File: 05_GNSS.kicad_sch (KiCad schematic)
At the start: 0 parts

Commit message: updated schematics
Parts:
- added U8: MAX-F10S-00B, MAX-F10S_UBL, symbol 2026-09-16_06-45-24:MAX-F10S-00B
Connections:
- new net GND: U8.1 (GND), U8.10 (GND), U8.12 (GND), U8.15 (VIO_SEL)
- new net GNSS_EXTINT: U8.5 (EXTINT)
- new net GNSS_RF: U8.11 (RF_IN)
- new net GNSS_TIMEPULSE: U8.4 (TIMEPULSE)
- new net GNSS_UART_RX: U8.3 (RXD)
- new net GNSS_UART_TX: U8.2 (TXD)
- new net VOUT1_1V8: U8.7 (V_IO)
- new net VOUT2_3V0_PROVISIONAL: U8.8 (VCC)
- no-connect marks 0 -> 7
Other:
- note added: "05_GNSS — u-blox MAX-F10S-00B DUAL-BAND GNSS — REV A"
- note added: "EXTINT is routed as an optional host signal for wake/time assistance. Final Apollo pin allocation may omit it if UART-RX wake is sufficient."
- note added: "Footprint field MAX-F10S_UBL is retained from the imported symbol; verify module pad geometry, pin-1 orientation and courtyard during the footprint audit."
- note added: "If VCC/V_IO are ever hard-switched off, Apollo pins connected to MAX-F10S must be Hi-Z first; do not drive GNSS I/O while its supplies are absent."
- note added: "MAX-F10S integrates L1/L5 SAW filtering + LNA + diplexer SAW, so do not duplicate an external SAW/LNA stage without a measured RF reason."
- note added: "POWER MANAGEMENT: prefer MAX-F10S software-standby when GNSS is idle. VCC and V_IO remain supplied, so host PIO isolation buffers are not required."
- note added: "POWER: VCC = VOUT2_3V0_PROVISIONAL (~3.0 V); V_IO = VOUT1_1V8; VIO_SEL = GND selects the 1.8 V I/O range."
- note added: "Primary host link = UART at 1.8 V logic. Passive L1/L5 antenna is the Rev-A baseline; RF network is finished on 14_RF."
- note added: "RESET_N is intentionally NC. u-blox recommends leaving it open for normal operation; do not add a capacitor to RESET_N. Reset also clears BBR/RTC/orbit data."
- note added: "RF_IN -> GNSS_RF. Route as controlled 50 ohm; RF_IN already contains a DC block. Keep this trace extremely short and away from display/Wi-Fi/high-speed clocks."
- note added: "SDA/SCL and SAFEBOOT_N are NC because UART is the primary host interface. LNA_EN and VCC_RF are NC for the passive-antenna baseline."
- note added: "TIMEPULSE is routed to GNSS_TIMEPULSE. Never load/pull it low during receiver startup because it is internally linked to SAFEBOOT_N."
- note added: "The 1.8 V V_IO rail must meet u-blox ±2% accuracy. VCC supply path must support up to 100 mA startup inrush and must not add >0.2 ohm series resistance."
- note added: "VOUT1_1V8 / VOUT2_3V0_PROVISIONAL and host/RF labels are local to this child sheet until the final hierarchy integration pass."
- note added: "V_BCKP is intentionally NC in Rev A. Host time/orbit assistance can be used instead; add a backup rail later only if TTFF measurements justify it."
- title: (none) -> Rev-A — GNSS

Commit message: refactor(kicad): integrate Rev-A hierarchy and libraries
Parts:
- U8: footprint MAX-F10S_UBL -> sportwatch_custom:MAX-F10S_UBL
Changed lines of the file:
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@@
 		)
 	)
-	(label "GNSS_TIMEPULSE"
+	(hierarchical_label "GNSS_TIMEPULSE"
+		(shape output)
 		(at 96 99.06 180)
 		(effects
@@
 		)
 	)
-	(label "VOUT1_1V8"
+	(hierarchical_label "VOUT1_1V8"
+		(shape passive)
 		(at 96 106.68 180)
 		(effects
@@
 		)
 	)
-	(label "VOUT2_3V0_PROVISIONAL"
+	(hierarchical_label "VOUT2_3V0_PROVISIONAL"
+		(shape passive)
 		(at 96 109.22 180)
 		(effects
@@
 		)
 	)
-	(label "GNSS_UART_RX"
+	(hierarchical_label "GNSS_UART_RX"
+		(shape input)
 		(at 96 96.52 180)
 		(effects
@@
 		)
 	)
-	(label "GNSS_UART_TX"
+	(hierarchical_label "GNSS_UART_TX"
+		(shape output)
 		(at 96 93.98 180)
 		(effects
@@
 		)
 	)
-	(label "GNSS_RF"
+	(hierarchical_label "GNSS_RF"
+		(shape passive)
 		(at 194 109.22 0)
 		(effects
@@
 		)
 	)
-	(label "GNSS_EXTINT"
+	(hierarchical_label "GNSS_EXTINT"
+		(shape input)
 		(at 96 101.6 180)
 		(effects
@@
 			)
 		)
-		(property "Footprint" "MAX-F10S_UBL"
+		(property "Footprint" "sportwatch_custom:MAX-F10S_UBL"
 			(at 111.76 91.44 0)
 			(hide yes)

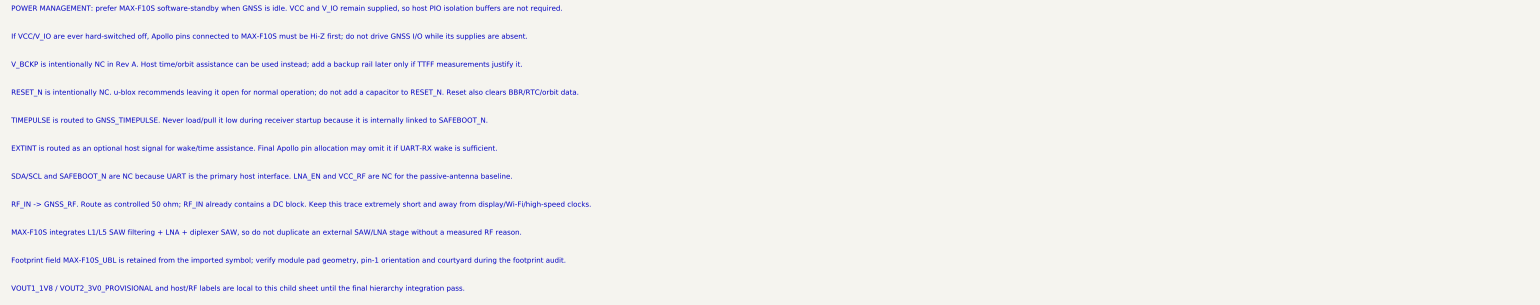
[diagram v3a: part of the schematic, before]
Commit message: fix(pcb): Round 3 foundation correction — 0 DRC errors, stacked microvias, PPG ECO & guards
- Eliminate 24 committed DRC errors by refilling all zones and committing refilled state
- Rebuild 12 L1->L3 skip microvias as 24 stackup-compliant stacked L1->L2 + L2->L3 microvias (VIPPO IPC-4761 Type VII)
- Harmonize HighSpeed_50R track width to 0.100 mm across .kicad_pro, .kicad_dru, and live copper
- Execute controlled schematic ECO swapping D413 and D424 detector channels, eliminating Jordan curve crossing
- Route all 4 PPG detector channels pad-to-pad on B.Cu with continuous dedicated PD_GND ground guards
- Close schematic residuals: Y101 MPN ABS07-32.768KHZ-6-T and 8.2pF load caps, cite primary sources for Y102 and Y1 on-chip trim, cite u-blox manual for U8 VCC_RF NC
- Formally defer staged passives (eMMC interface, PPG VLED, C206) with documented reserved placement corridors
- Document comprehensive Round 3 report and update Apollo/eMMC escape matrices and AGENT_HANDOFF.md
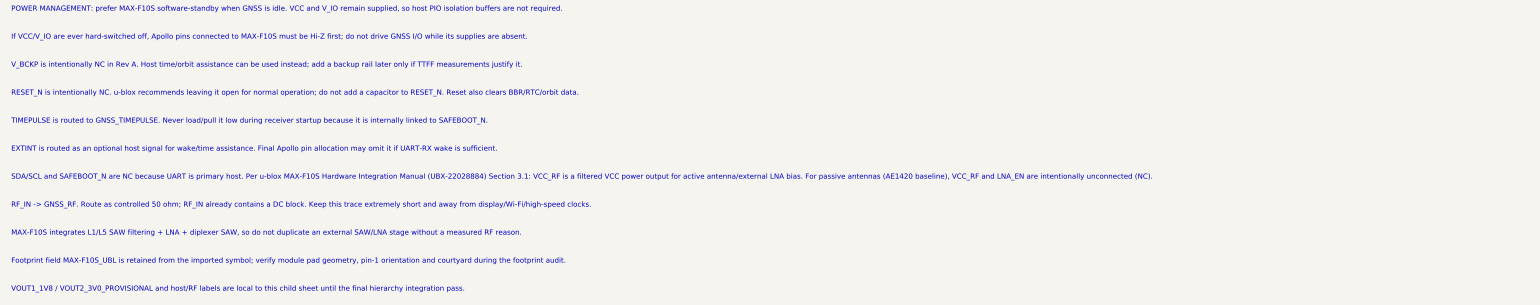
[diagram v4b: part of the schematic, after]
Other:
- note added: "SDA/SCL and SAFEBOOT_N are NC because UART is primary host. Per u-blox MAX-F10S Hardware Integration Manual (UBX-22028884) Section 3.1: VCC_RF is a filtered VCC power output for active antenna/external LNA bias. For passive antennas (AE1420 baseline), VCC_RF and LNA_EN are intentionally unconnected (NC)."
- note removed: "SDA/SCL and SAFEBOOT_N are NC because UART is the primary host interface. LNA_EN and VCC_RF are NC for the passive-antenna baseline."
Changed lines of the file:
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@@
 		)
 	)
-	(text "SDA/SCL and SAFEBOOT_N are NC because UART is the primary host interface. LNA_EN and VCC_RF are NC for the passive-antenna baseline."
+	(text "SDA/SCL and SAFEBOOT_N are NC because UART is primary host. Per u-blox MAX-F10S Hardware Integration Manual (UBX-22028884) Section 3.1: VCC_RF is a filtered VCC power output for active antenna/external LNA bias. For passive antennas (AE1420 baseline), VCC_RF and LNA_EN are intentionally unconnected (NC)."
 		(exclude_from_sim no)
 		(at 24 176 0)

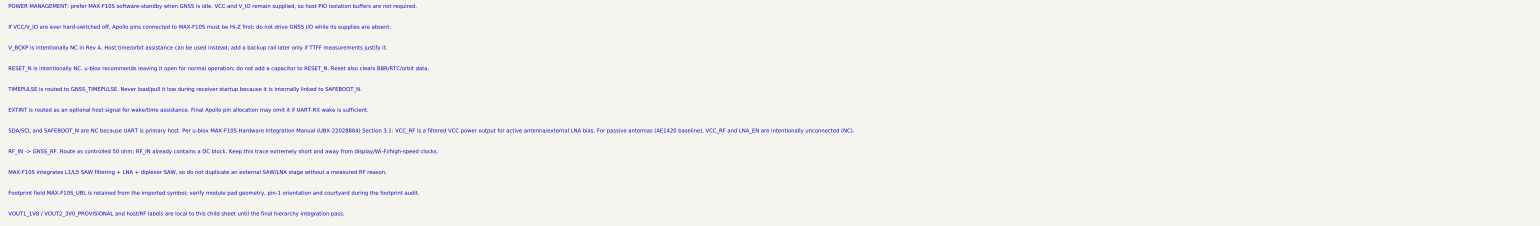
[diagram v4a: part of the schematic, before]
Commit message: fix(pcb): foundation correction round 4 closure
- Y101: select Abracon ABS06-32.768KHZ-6-1-T (2012-class SMD crystal) matching 2012 footprint
- Y101/C118/C119: rotate Y101 180 deg to align XO32 West and XI32 East; uncrossed planar routing
- Parity: synchronize C118, C119, Y101, Y102, Y1 values between schematic and PCB (0 mismatches)
- PPG guards: close NT401.2 and NT402.2 to In6.Cu GND plane via B.Cu microvias (4 channels complete)
- Rules: reconcile HighSpeed_50R track_width to 0.100 mm in .kicad_pro; refine *1V8* to *VOUT*1V8*
- GNSS: update note to cite MAX-F10S Integration Manual UBXDOC-963802114-12892 R01 and south RF_IN
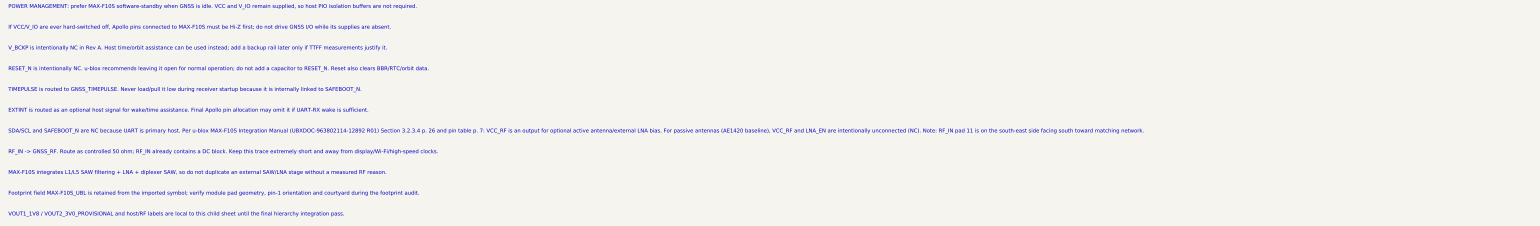
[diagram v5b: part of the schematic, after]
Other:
- note added: "SDA/SCL and SAFEBOOT_N are NC because UART is primary host. Per u-blox MAX-F10S Integration Manual (UBXDOC-963802114-12892 R01) Section 3.2.3.4 p. 26 and pin table p. 7: VCC_RF is an output for optional active antenna/external LNA bias. For passive antennas (AE1420 baseline), VCC_RF and LNA_EN are intentionally unconnected (NC). Note: RF_IN pad 11 is on the south-east side facing south toward mat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"
- note removed: "SDA/SCL and SAFEBOOT_N are NC because UART is primary host. Per u-blox MAX-F10S Hardware Integration Manual (UBX-22028884) Section 3.1: VCC_RF is a filtered VCC power output for active antenna/external LNA bias. For passive antennas (AE1420 baseline), VCC_RF and LNA_EN are intentionally unconnected (NC)."
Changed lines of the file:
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@@
 		)
 	)
-	(text "SDA/SCL and SAFEBOOT_N are NC because UART is primary host. Per u-blox MAX-F10S Hardware Integration Manual (UBX-22028884) Section 3.1: VCC_RF is a filtered VCC power output for active antenna/external LNA bias. For passive antennas (AE1420 baseline), VCC_RF and LNA_EN are intentionally unconnected (NC)."
+	(text "SDA/SCL and SAFEBOOT_N are NC because UART is primary host. Per u-blox MAX-F10S Integration Manual (UBXDOC-963802114-12892 R01) Section 3.2.3.4 p. 26 and pin table p. 7: VCC_RF is an output for optional active antenna/external LNA bias. For passive antennas (AE1420 baseline), VCC_RF and LNA_EN are intentionally unconnected (NC). Note: RF_IN pad 11 is on the south-east side facing south toward matching network."
 		(exclude_from_sim no)
 		(at 24 176 0)

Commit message: fix(pcb): foundation correction round 5 closure
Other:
- note added: "SDA/SCL and SAFEBOOT_N are NC because UART is primary host. Per u-blox MAX-F10S Integration Manual (UBXDOC-963802114-12892 R01) Section 3.2.3.4 p. 26 and pin table p. 7: VCC_RF is an output for optional active antenna/external LNA bias. For passive antennas (AE1420 baseline), VCC_RF and LNA_EN are intentionally unconnected (NC). Note: In KiCad normal top view (lower Y = north/up), U8 center is at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"
- note removed: "SDA/SCL and SAFEBOOT_N are NC because UART is primary host. Per u-blox MAX-F10S Integration Manual (UBXDOC-963802114-12892 R01) Section 3.2.3.4 p. 26 and pin table p. 7: VCC_RF is an output for optional active antenna/external LNA bias. For passive antennas (AE1420 baseline), VCC_RF and LNA_EN are intentionally unconnected (NC). Note: RF_IN pad 11 is on the south-east side facing south toward mat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"
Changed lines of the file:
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@@
 		)
 	)
-	(text "SDA/SCL and SAFEBOOT_N are NC because UART is primary host. Per u-blox MAX-F10S Integration Manual (UBXDOC-963802114-12892 R01) Section 3.2.3.4 p. 26 and pin table p. 7: VCC_RF is an output for optional active antenna/external LNA bias. For passive antennas (AE1420 baseline), VCC_RF and LNA_EN are intentionally unconnected (NC). Note: RF_IN pad 11 is on the south-east side facing south toward matching network."
+	(text "SDA/SCL and SAFEBOOT_N are NC because UART is primary host. Per u-blox MAX-F10S Integration Manual (UBXDOC-963802114-12892 R01) Section 3.2.3.4 p. 26 and pin table p. 7: VCC_RF is an output for optional active antenna/external LNA bias. For passive antennas (AE1420 baseline), VCC_RF and LNA_EN are intentionally unconnected (NC). Note: In KiCad normal top view (lower Y = north/up), U8 center is at ~(100, 86) and RF_IN pad 11 is at ~(103.30, 81.11) on the north-east side, facing north toward the matching network at Y ~ 79.2 (historical south/south-east wording SUPERSEDED)."
 		(exclude_from_sim no)
 		(at 24 176 0)

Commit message: foundation correction
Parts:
- U8: Board (none) -> MAIN
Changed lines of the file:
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@@
 			)
 		)
-	)
+(property "Board" "MAIN" (at 0 0 0) (effects (font (size 1 1)) (hide yes)))
+)
 	(symbol
 		(lib_id "power:GND")
@@
 			)
 		)
-	)
+(property "Board" "MAIN" (at 0 0 0) (effects (font (size 1 1)) (hide yes)))
+)
 	(symbol
 		(lib_id "power:GND")
@@
 			)
 		)
-	)
+(property "Board" "MAIN" (at 0 0 0) (effects (font (size 1 1)) (hide yes)))
+)
 	(symbol
 		(lib_id "power:GND")
@@
 			)
 		)
-	)
+(property "Board" "MAIN" (at 0 0 0) (effects (font (size 1 1)) (hide yes)))
+)
 	(symbol
 		(lib_id "2026-09-16_06-45-24:MAX-F10S-00B")
@@
 			)
 		)
-	)
-)
+(property "Board" "MAIN" (at 0 0 0) (effects (font (size 1 1)) (hide yes)))
+)
+)
